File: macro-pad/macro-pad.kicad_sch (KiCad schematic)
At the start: 30 parts, among them J1 USB_C_Receptacle_USB2.0, J2 Conn_01x04, J8 Conn_01x06, Q1 2N7002, U1 USBLC6-2SC6, U2 ATmega32U4-AU, Y1 Crystal_GND24

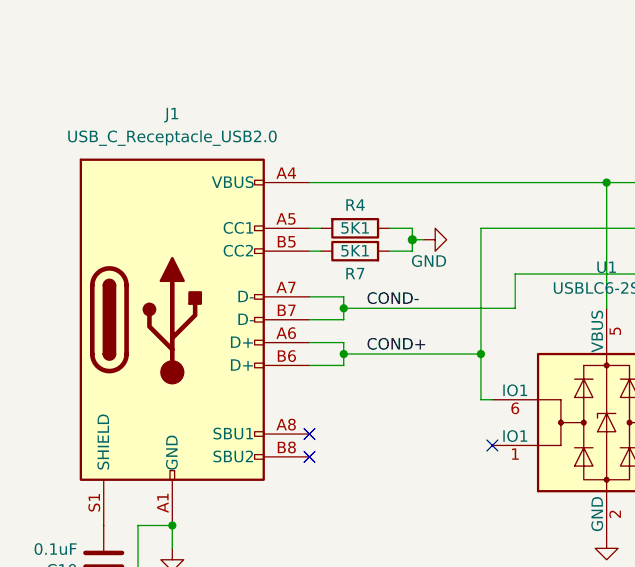
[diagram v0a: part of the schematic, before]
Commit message: add case plates generation
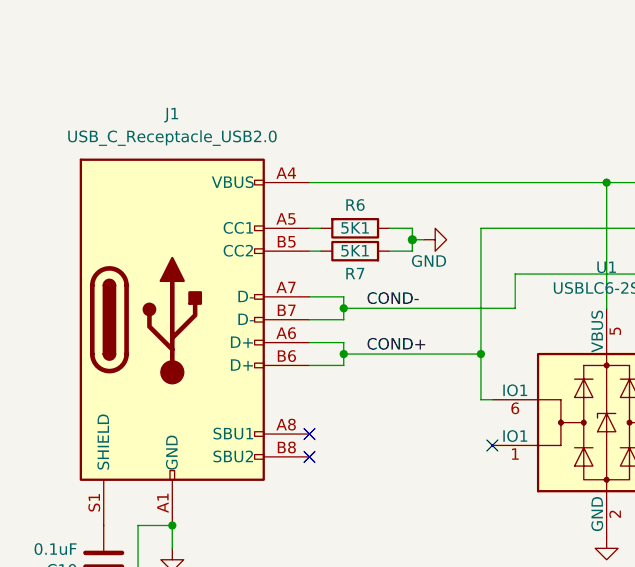
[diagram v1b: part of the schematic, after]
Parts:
- H1, H2, H3, H4, H5: footprint MountingHole:MountingHole_3.2mm_M3 -> keeb-conn:MountingHole_3.2mm_M3
- renumbered R4 to R6
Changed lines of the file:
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@@
 (kicad_sch
-	(version 20231120)
+	(version 20250114)
 	(generator "eeschema")
-	(generator_version "8.0")
+	(generator_version "9.0")
 	(paper "A4")
 	(title_block
@@
 	(label "SCK"
 		(at 165.1 72.39 0)
-		(fields_autoplaced yes)
 		(effects
 			(font
@@
 	(label "col2"
 		(at 198.12 93.98 0)
-		(fields_autoplaced yes)
 		(effects
 			(font
@@
 	(label "col1"
 		(at 198.12 91.44 0)
-		(fields_autoplaced yes)
 		(effects
 			(font
@@
 	(label "col4"
 		(at 179.07 92.71 0)
-		(fields_autoplaced yes)
 		(effects
 			(font
@@
 	(label "MISO"
 		(at 153.67 77.47 0)
-		(fields_autoplaced yes)
 		(effects
 			(font
@@
 	(label "col4"
 		(at 198.12 99.06 0)
-		(fields_autoplaced yes)
 		(effects
 			(font
@@
 	(label "col9"
 		(at 198.12 111.76 0)
-		(fields_autoplaced yes)
 		(effects
 			(font
@@
 	(label "col14"
 		(at 198.12 124.46 0)
-		(fields_autoplaced yes)
 		(effects
 			(font
@@
 	(label "enc1"
 		(at 179.07 135.89 0)
-		(fields_autoplaced yes)
 		(effects
 			(font
@@
 	(label "ledGND"
 		(at 179.07 144.78 0)
-		(fields_autoplaced yes)
 		(effects
 			(font
@@
 	(label "row2"
 		(at 179.07 105.41 0)
-		(fields_autoplaced yes)
 		(effects
 			(font
@@
 	(label "enc1"
 		(at 198.755 127 0)
-		(fields_autoplaced yes)
 		(effects
 			(font
@@
 	(label "SCK"
 		(at 97.79 33.02 0)
-		(fields_autoplaced yes)
 		(effects
 			(font
@@
 	(label "MOSI"
 		(at 153.67 74.93 0)
-		(fields_autoplaced yes)
 		(effects
 			(font
@@
 	(label "col7"
 		(at 198.12 106.68 0)
-		(fields_autoplaced yes)
 		(effects
 			(font
@@
 	(label "col8"
 		(at 179.07 69.85 0)
-		(fields_autoplaced yes)
 		(effects
 			(font
@@
 	(label "col7"
 		(at 179.07 72.39 0)
-		(fields_autoplaced yes)
 		(effects
 			(font
@@
 	(label "SCK"
 		(at 153.67 72.39 0)
-		(fields_autoplaced yes)
 		(effects
 			(font
@@
 	(label "col8"
 		(at 198.12 109.22 0)
-		(fields_autoplaced yes)
 		(effects
 			(font
@@
 	(label "row3"
 		(at 198.12 78.74 0)
-		(fields_autoplaced yes)
 		(effects
 			(font
@@
 	(label "col10"
 		(at 177.8 82.55 0)
-		(fields_autoplaced yes)
 		(effects
 			(font
@@
 	(label "row0"
 		(at 198.12 71.12 0)
-		(fields_autoplaced yes)
 		(effects
 			(font
@@
 	(label "col1"
 		(at 179.07 133.35 0)
-		(fields_autoplaced yes)
 		(effects
 			(font
@@
 	(label "COND-"
 		(at 48.26 154.94 0)
-		(fields_autoplaced yes)
 		(effects
 			(font
@@
 	(label "row1"
 		(at 198.12 73.66 0)
-		(fields_autoplaced yes)
 		(effects
 			(font
@@
 	(label "row3"
 		(at 179.07 107.95 0)
-		(fields_autoplaced yes)
 		(effects
 			(font
@@
 	(label "enc2"
 		(at 179.07 138.43 0)
-		(fields_autoplaced yes)
 		(effects
 			(font
@@
 	(label "col2"
 		(at 179.07 125.73 0)
-		(fields_autoplaced yes)
 		(effects
 			(font
@@
 	(label "MOSI"
 		(at 97.79 38.1 0)
-		(fields_autoplaced yes)
 		(effects
 			(font
@@
 	(label "col12"
 		(at 177.8 118.11 0)
-		(fields_autoplaced yes)
 		(effects
 			(font
@@
 	(label "row2"
 		(at 198.12 76.2 0)
-		(fields_autoplaced yes)
 		(effects
 			(font
@@
 	(label "col0"
 		(at 179.07 130.81 0)
-		(fields_autoplaced yes)
 		(effects
 			(font
@@
 	(label "row4"
 		(at 179.07 113.03 0)
-		(fields_autoplaced yes)
 		(effects
 			(font
@@
 	(label "row4"
 		(at 198.12 81.28 0)
-		(fields_autoplaced yes)
 		(effects
 			(font
@@
 	(label "col3"
 		(at 198.12 96.52 0)
-		(fields_autoplaced yes)
 		(effects
 			(font
@@
 	(label "~{RES}"
 		(at 97.79 43.18 0)
-		(fields_autoplaced yes)
 		(effects
 			(font
@@
 	(label "enc2"
 		(at 199.39 129.54 0)
-		(fields_autoplaced yes)
 		(effects
 			(font
@@
 	(label "col6"
 		(at 179.07 110.49 0)
-		(fields_autoplaced yes)
 		(effects
 			(font
@@
 	(label "row5"
 		(at 179.07 141.605 0)
-		(fields_autoplaced yes)
 		(effects
 			(font
@@
 	(label "row1"
 		(at 179.07 102.87 0)
-		(fields_autoplaced yes)
 		(effects
 			(font
@@
 	(label "col3"
 		(at 179.07 95.25 0)
-		(fields_autoplaced yes)
 		(effects
 			(font
@@
 	(label "col0"
 		(at 198.12 88.9 0)
-		(fields_autoplaced yes)
 		(effects
 			(font
@@
 	(label "MISO"
 		(at 165.1 77.47 0)
-		(fields_autoplaced yes)
 		(effects
 			(font
@@
 	(label "ledGND"
 		(at 198.12 137.16 0)
-		(fields_autoplaced yes)
 		(effects
 			(font
@@
 	(label "col9"
 		(at 179.07 87.63 0)
-		(fields_autoplaced yes)
 		(effects
 			(font
@@
 	(label "col11"
 		(at 177.8 80.01 0)
-		(fields_autoplaced yes)
 		(effects
 			(font
@@
 	(label "col5"
 		(at 198.12 101.6 0)
-		(fields_autoplaced yes)
 		(effects
 			(font
@@
 	(label "col10"
 		(at 198.12 114.3 0)
-		(fields_autoplaced yes)
 		(effects
 			(font
@@
 	(label "col13"
 		(at 177.8 115.57 0)
-		(fields_autoplaced yes)
 		(effects
 			(font
@@
 	(label "row5"
 		(at 198.12 83.82 0)
-		(fields_autoplaced yes)
 		(effects
 			(font
@@
 	(label "col14"
 		(at 177.8 77.47 0)
-		(fields_autoplaced yes)
 		(effects
 			(font
@@
 	(label "row0"
 		(at 179.07 100.33 0)
-		(fields_autoplaced yes)
 		(effects
 			(font
@@
 	(label "col13"
 		(at 198.12 121.92 0)
-		(fields_autoplaced yes)
 		(effects
 			(font
@@
 	(label "col6"
 		(at 198.12 104.14 0)
-		(fields_autoplaced yes)
 		(effects
 			(font
@@
 	(label "MISO"
 		(at 97.79 22.86 0)
-		(fields_autoplaced yes)
 		(effects
 			(font
@@
 	(label "COND+"
 		(at 48.26 160.02 0)
-		(fields_autoplaced yes)
 		(effects
 			(font
@@
 	(label "col5"
 		(at 179.07 85.09 0)
-		(fields_autoplaced yes)
 		(effects
 			(font
@@
 	(label "col11"
 		(at 198.12 116.84 0)
-		(fields_autoplaced yes)
 		(effects
 			(font
@@
 	(label "col12"
 		(at 198.12 119.38 0)
-		(fields_autoplaced yes)
 		(effects
 			(font
@@
 			)
 		)
-		(property "Footprint" "MountingHole:MountingHole_3.2mm_M3"
+		(property "Footprint" "keeb-conn:MountingHole_3.2mm_M3"
 			(at 236.22 68.58 0)
 			(effects
@@
 			)
 		)
-		(property "Footprint" "MountingHole:MountingHole_3.2mm_M3"
+		(property "Footprint" "keeb-conn:MountingHole_3.2mm_M3"
 			(at 236.22 73.66 0)
 			(effects
@@
 			)
 		)
-		(property "Footprint" "MountingHole:MountingHole_3.2mm_M3"
+		(property "Footprint" "keeb-conn:MountingHole_3.2mm_M3"
 			(at 236.22 78.74 0)
 			(effects
@@
 			)
 		)
-		(property "Footprint" "MountingHole:MountingHole_3.2mm_M3"
+		(property "Footprint" "keeb-conn:MountingHole_3.2mm_M3"
 			(at 236.22 83.82 0)
 			(effects
@@
 			)
 		)
-		(property "Footprint" "MountingHole:MountingHole_3.2mm_M3"
+		(property "Footprint" "keeb-conn:MountingHole_3.2mm_M3"
 			(at 236.22 88.9 0)
 			(effects
@@
 		(on_board yes)
 		(dnp no)
-		(property "Reference" "R4"
+		(property "Reference" "R6"
 			(at 46.99 143.51 90)
 			(effects
@@
 		(on_board yes)
 		(dnp no)
-		(property "Reference" "#PWR016"
+		(property "Reference" "#PWR02"
 			(at 60.96 147.32 0)
 			(effects
@@
 		(at 205.74 67.31)
 		(size 20.32 77.47)
+		(exclude_from_sim no)
+		(in_bom yes)
+		(on_board yes)
+		(dnp no)
 		(fields_autoplaced yes)
 		(stroke
@@
 		)
 	)
+	(embedded_fonts no)
 )
